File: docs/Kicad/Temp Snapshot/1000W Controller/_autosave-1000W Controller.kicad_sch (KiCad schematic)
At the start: 58 parts, among them Q2 Q_PMOS_GSD, Q3 Q_NMOS_GSD, U1 ADuM1201AR, U2 R-783.3-0.5, U3 LD1117V, U4 ADuM1201AR, U5 ADuM1201AR, U6 ADuM1201AR

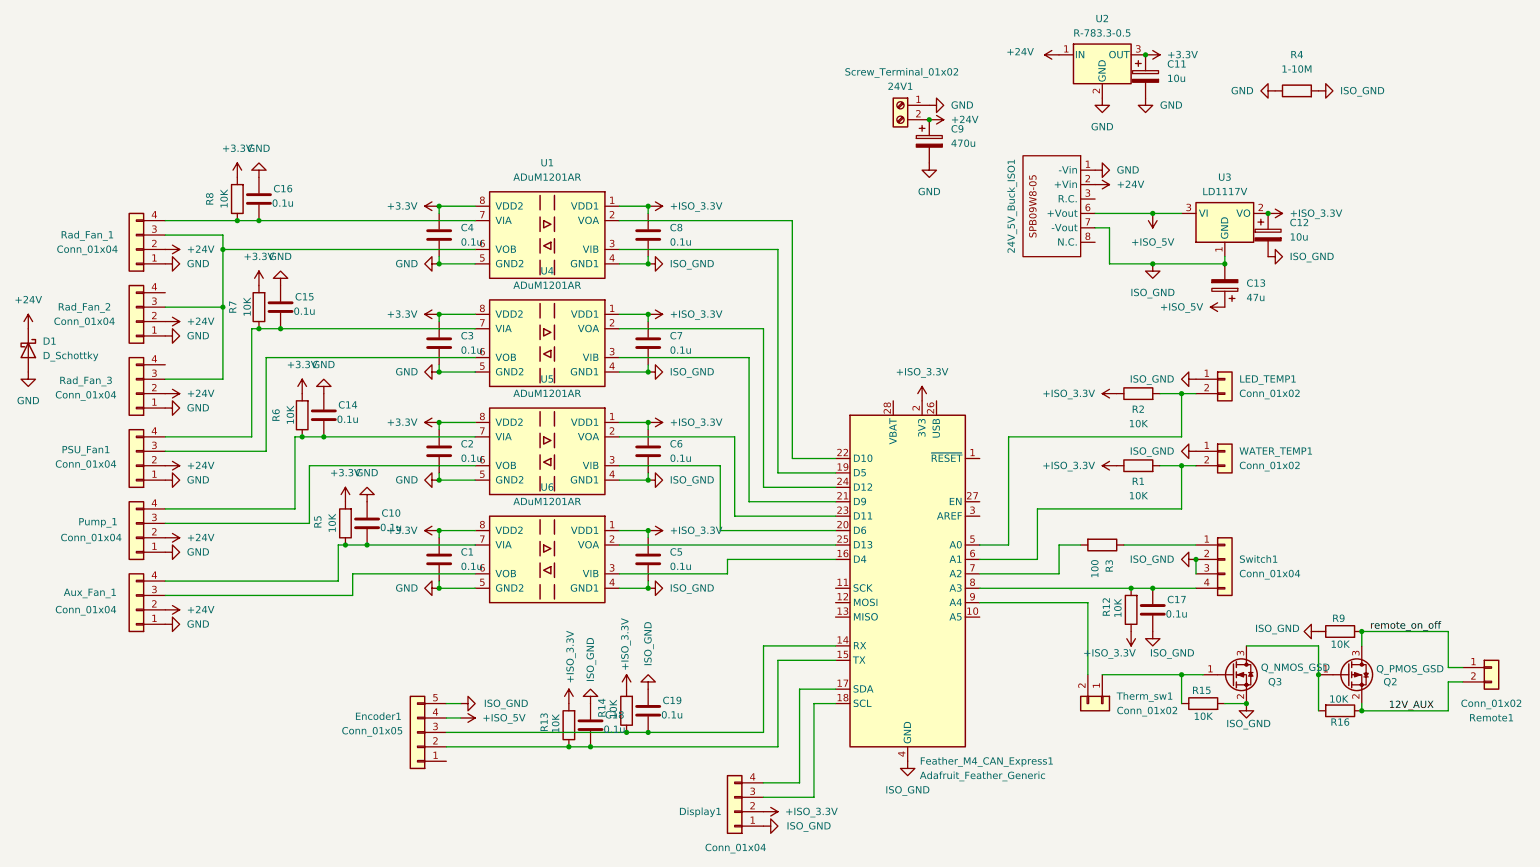
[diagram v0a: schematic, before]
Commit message: Per-channel fault ignoring, cooling/PSU control overhaul, docs refresh
Replaces the old global "unsafe mode" bypass with per-channel fault
ignoring: a 3s hold in ERROR_KILL now permanently silences only the
specific channel at fault (of 8: LED/water temp, pump, main/PSU/aux
fan, PSU comms, encoder), not all fault checking. Fixes the long-
standing 0-RPM tach bug (a redundant pinMode() call was clobbering the
EIC pin-mux after interrupt attachment). Reworks CoolingService: main
fan now runs the sole PI loop, targeting water temp; PSU/aux fans
track LED duty with a fixed linear ratio; pump duty is now a flat
constant with no PI loop. Adds a 110% LED current overclock
(MAX_LED_CURRENT_A), peak-RPM diagnostics, and two bench-test
firmwares (aux_fan_bench, all_tach_bench) used to isolate hardware
issues. Updates Firmware_Architecture.md, Electronics_Architecture.md,
and Error_Codes.md to match, including a newly-found analog-mode
current ceiling (~23.15A, rail-limited) below the configured 24.2A.

Co-Authored-By: Claude Sonnet 5 <noreply@anthropic.com>
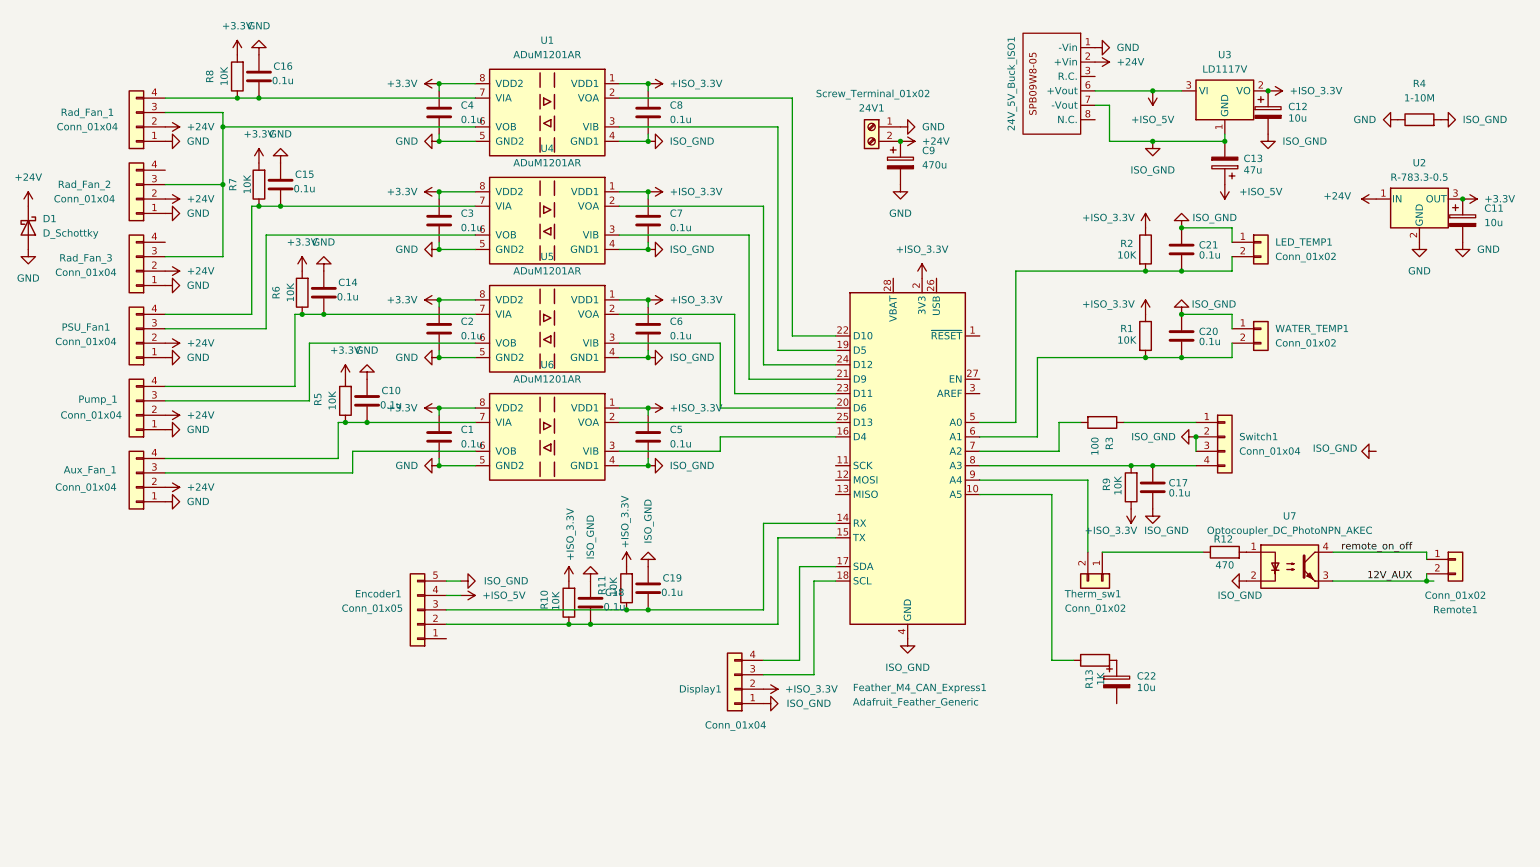
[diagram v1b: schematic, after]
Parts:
- removed Q2: Q_PMOS_GSD, Package_TO_SOT_SMD:SOT-23, symbol Transistor_FET:Q_PMOS_GSD
- removed Q3: Q_NMOS_GSD, Package_TO_SOT_SMD:SOT-23, symbol Transistor_FET:Q_NMOS_GSD
- removed R16, R9: 10K, Resistor_SMD:R_0805_2012Metric, symbol Device:R
- added C20, C21: 0.1u, Capacitor_SMD:C_0805_2012Metric, symbol Device:C
- added C22: 10u, Capacitor_SMD:C_0805_2012Metric, symbol Device:C_Polarized
- added R13: 1K, Resistor_SMD:R_0805_2012Metric, symbol Device:R
- added U7: Optocoupler_DC_PhotoNPN_AKEC, Package_DIP:DIP-4_W7.62mm, symbol Isolator:Optocoupler_DC_PhotoNPN_AKEC
- R12: renamed from R15; value 10K -> 470
- renumbered R13 to R10, R14 to R11, R12 to R9
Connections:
- net 12V_AUX: now also U7.3
- net ISO_GND: now also C20.1, C21.1, U7.2; no longer R12.2
- net remote_on_off: now also U7.4
- net at Feather_M4_CAN_Express1.6 (A1), R1.2, WATER_TEMP1.2 (Pin_2): now also C20.2
- net at Feather_M4_CAN_Express1.10 (A5): now also R13.1
- net at Feather_M4_CAN_Express1.5 (A0), LED_TEMP1.2 (Pin_2), R2.2: now also C21.2
- new net: R12.2, U7.1
- new net: C22.1, R13.2
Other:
- moved on the sheet: 24V1, 24V_5V_Buck_ISO1, Aux_Fan_1, C1, C10, C11, C12, C13, C14, C15, C16, C17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
